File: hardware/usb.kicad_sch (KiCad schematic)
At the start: 0 parts

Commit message: added USB components, updated BOM, marked components that still needs references
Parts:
- added C266, C267, C268, C269, C270, C271: C, symbol Device:C
- added IC30: USB3340-EZK-TR, QFN50P500X500X100-33N-D, symbol payload-sym:USB3340-EZK-TR
- added IC31: TPS2051BDGN, SOP65P490X110-9N, symbol payload-sym:TPS2051BDGN
- added IC32: PTN5150AHXMP, PTN5150AHXMP, symbol payload-sym:PTN5150AHXMP
- added J1: USB-C_Mtconn_UBF31-0171, USB-C_Mtconn_UBF31-0171, symbol payload-sym:USB-C_Mtconn_UBF31-0171
- added R155, R156, R157, R158, R159, R160, R161, R162, R163, R164, R165: R_US, symbol Device:R_US
- added TP31, TP32, TP33, TP34: TestPoint, symbol Connector:TestPoint
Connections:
- new net: J1.A1 (GND), J1.A12 (GND), J1.B1 (GND), J1.B12 (GND)
- new net: J1.A4 (VBUS), J1.A9 (VBUS), J1.B4 (VBUS), J1.B9 (VBUS)
- new net: C267.1, IC32.4 (VBUS_DET), R163.1
- new net: IC30.1 (CLKOUT), R164.2
- new net: IC32.3 (PORT), R156.2, R162.1
- new net: C271.1, IC30.28 (VDD18), IC30.30 (NC_2)
- new net: C269.1, IC30.20 (VDD33)
- new net: IC30.24 (RBIAS), R165.2
- new net 3V3_USB0_RESETB: IC30.27 (RESETB)
- new net ADR/COM_DET: IC30.2 (NXT), IC32.5 (ADR/CON_DET), R157.2, R161.1, R164.1, TP31.1
- new net GNDREF: C266.2, C267.2, C268.2, C269.2, C270.2, C271.2, IC30.33 (EPAD), IC32.10 (GND), R161.2, R162.2, R165.1
- new net INTB/OUT3: IC30.3 (DATA0), IC32.6 (INTB/OUT3), R158.2, TP32.1
- new net SCL_OUT2: IC30.10 (DATA6), IC30.13 (DATA7), IC30.5 (DATA2), IC30.7 (DATA4), IC32.8 (SCL/OUT2), R160.2, TP34.1
- new net SDA_OUT1: IC30.4 (DATA1), IC30.6 (DATA3), IC30.9 (DATA5), IC32.7 (SDA/OUT1), R159.2, TP33.1
- new net SYS_5V: C270.1, IC30.21 (VBAT)
- new net USB0_CC1: IC32.1 (CC1)
- new net USB0_CC2: IC32.2 (CC2)
- new net USB0_DIR: IC30.31 (DIR)
- new net USB0_ID: IC30.23 (ID), IC32.9 (ID), R155.2
- new net USB0_STP: IC30.29 (STP)
- new net USB0_VBUS: IC30.22 (VBUS)
- new net USB_5V: R163.2
- new net VCC_3V3: C266.1, C268.1, IC30.32 (VDDIO), IC32.12 (VDD), R155.1, R156.1, R157.1, R158.1, R159.1, R160.1

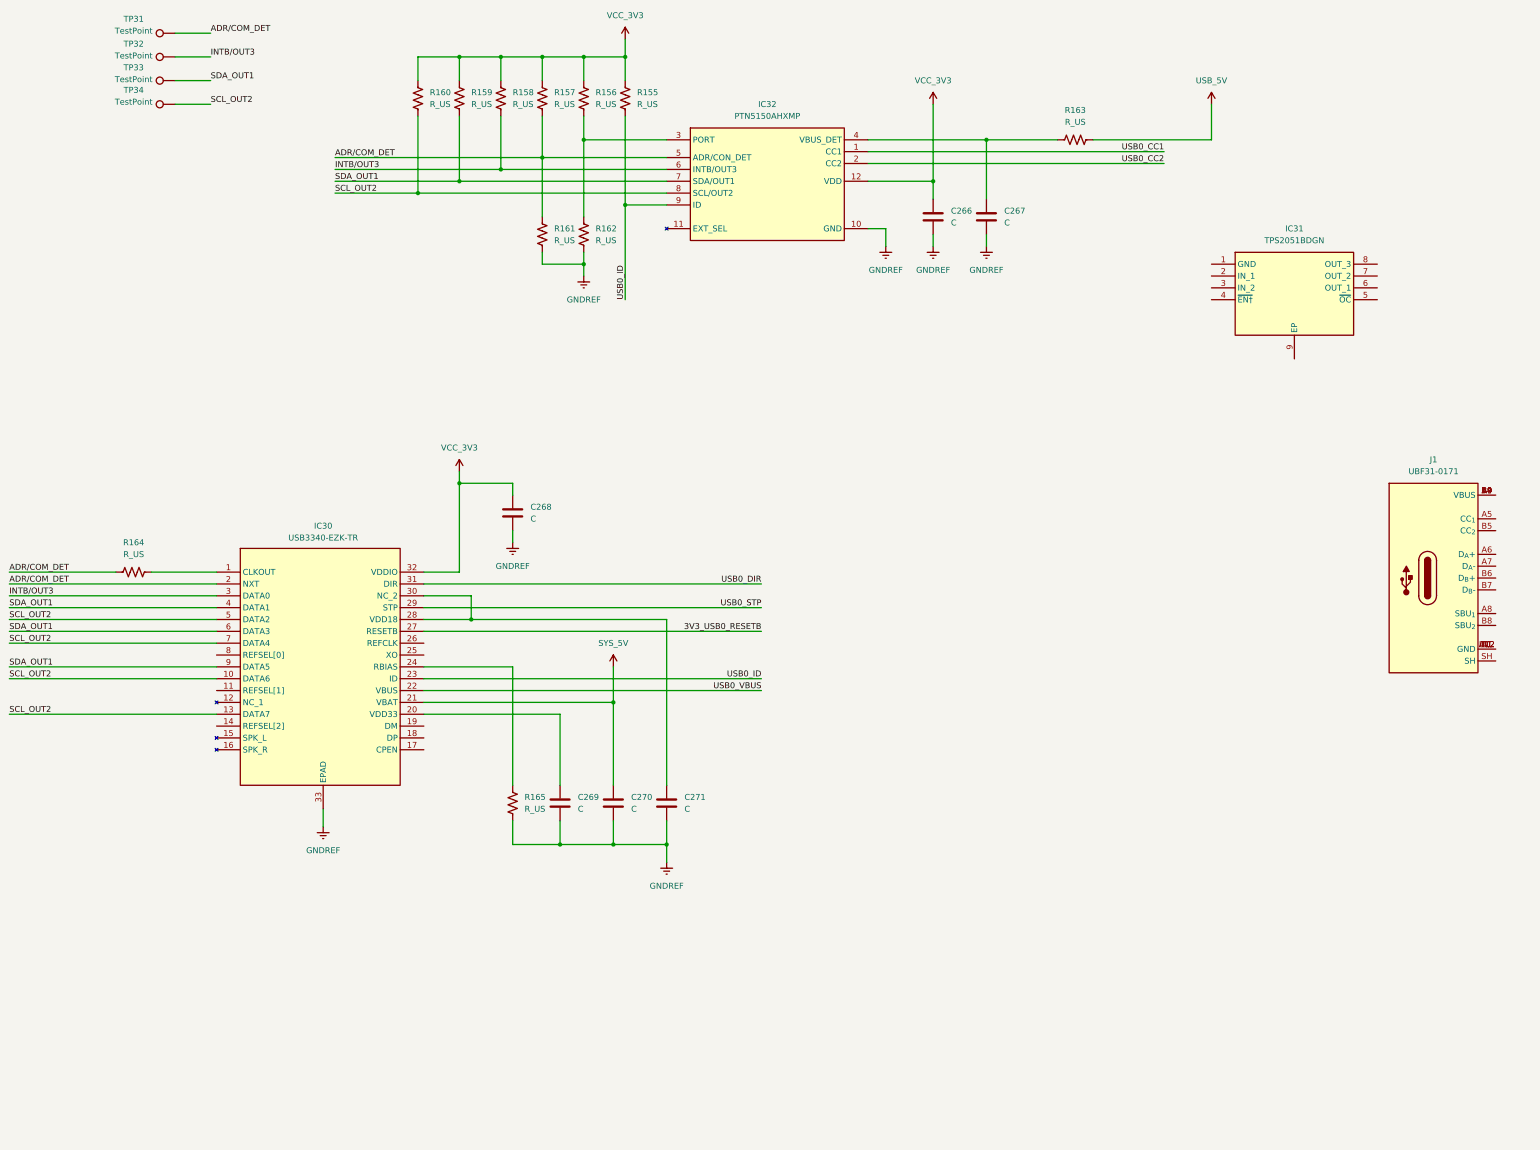
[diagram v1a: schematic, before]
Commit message: added usb devices in schematics
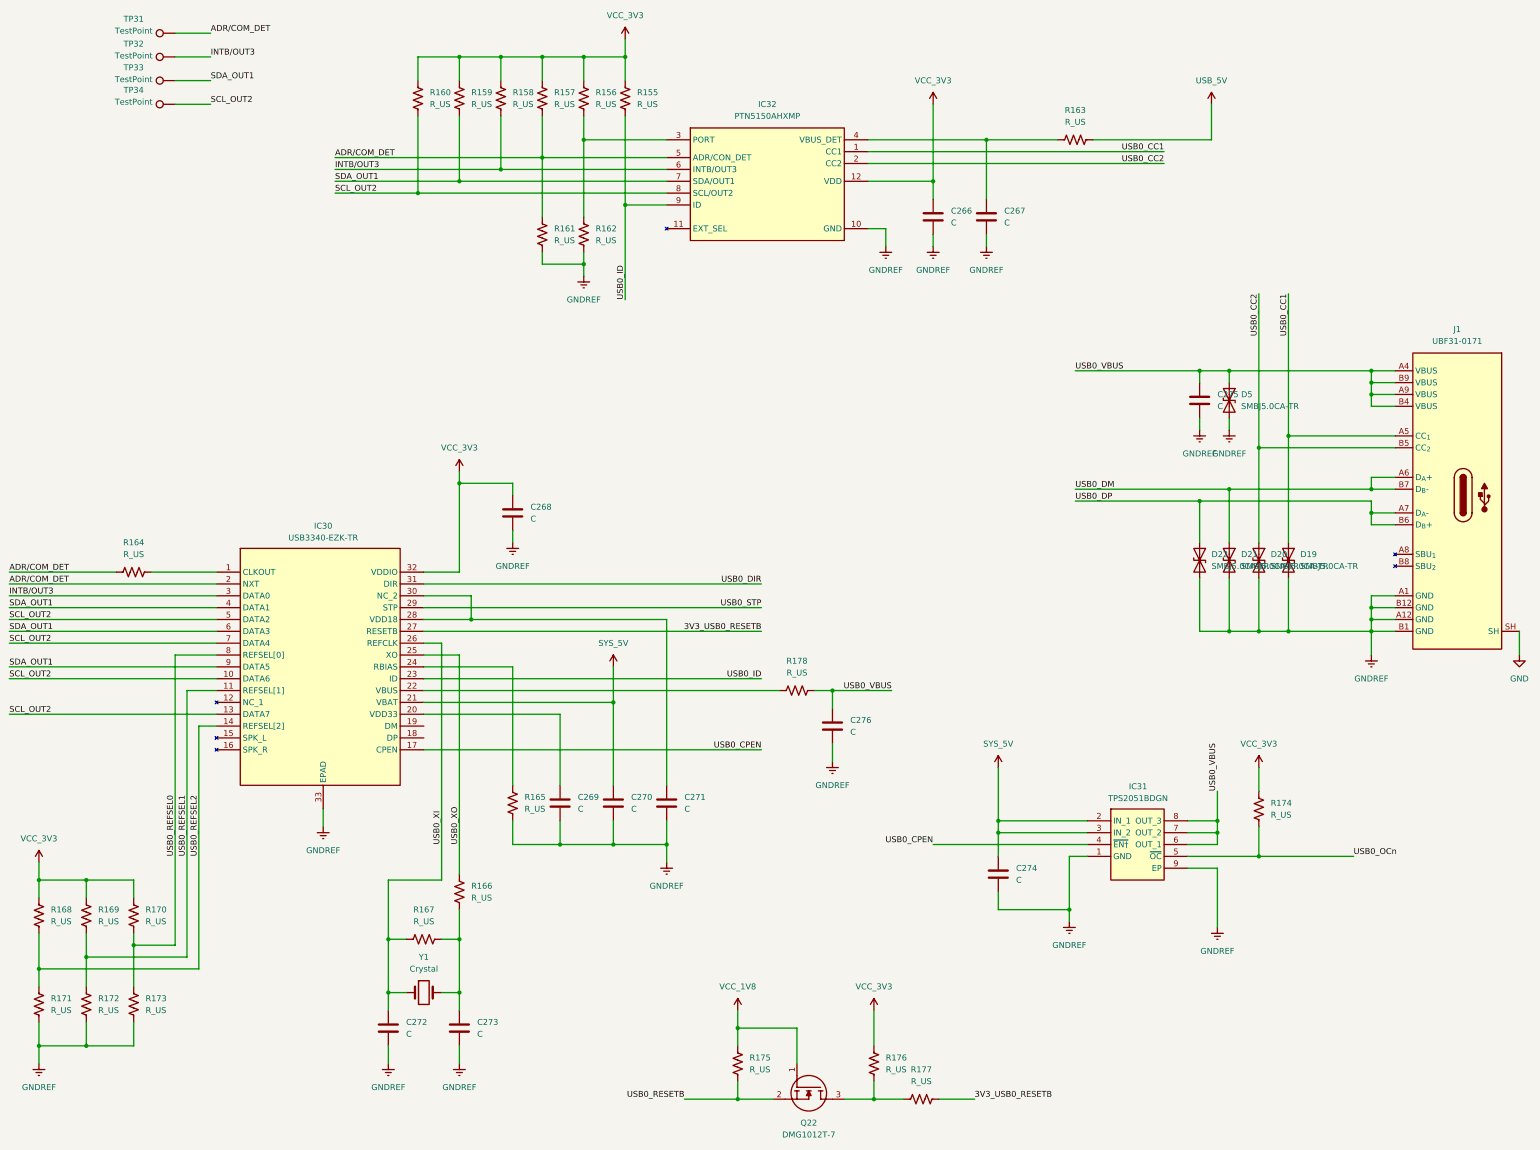
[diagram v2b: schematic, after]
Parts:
- added C272, C273, C274, C275, C276: C, symbol Device:C
- added D19, D20, D21, D22, D5: SMBJ5.0CA-TR, payload_footprints:SMBJ12A, symbol Device:D_TVS
- added Q22: DMG1012T-7, SOT50P160X90-3N, symbol payload-sym:DMG1012T-7
- added R166, R167, R168, R169, R170, R171, R172, R173, R174, R175, R176, R177, R178: R_US, symbol Device:R_US
- added Y1: Crystal, symbol Device:Crystal
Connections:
- net 3V3_USB0_RESETB: now also R177.1
- net GNDREF: now also IC31.1 (GND), IC31.9 (EP), J1.A1 (GND), J1.A12 (GND), J1.B1 (GND), J1.B12 (GND), C272.2, C273.2, C274.2, C275.2, C276.2, D19.2 (A2), D20.2 (A2), D21.2 (A2), D22.2 (A2), D5.2 (A2), R171.1, R172.1, R173.1
- net SYS_5V: now also IC31.2 (IN_1), IC31.3 (IN_2), C274.1
- net USB0_CC1: now also J1.A5 (CC_{1}), D19.1 (A1)
- net USB0_CC2: now also J1.B5 (CC_{2}), D20.1 (A1)
- net USB0_VBUS: now also IC31.6 (OUT_1), IC31.7 (OUT_2), IC31.8 (OUT_3), J1.A4 (VBUS), J1.A9 (VBUS), J1.B4 (VBUS), J1.B9 (VBUS), C275.1, C276.1, D5.1 (A1), R178.1; no longer IC30.22 (VBUS)
- net VCC_3V3: now also R168.2, R169.2, R170.2, R174.2, R176.2
- net USB0_DM: now reaches J1.A6 (D_{A}+)
- net USB0_DM: now also J1.B7 (D_{B}-), D21.1 (A1)
- net USB0_DP: now reaches J1.A7 (D_{A}-)
- net USB0_DP: now also J1.B6 (D_{B}+), D22.1 (A1)
- net GND: now reaches J1.SH
- net USB0_CPEN: now reaches IC31.4 (~{EN†})
- net USB0_CPEN: now also IC30.17 (CPEN)
- net USB0_OCn: now reaches IC31.5 (~{OC})
- net USB0_OCn: now also R174.1
- net USB0_REFSEL1: now reaches IC30.11 (REFSEL[1])
- net USB0_REFSEL1: now also R169.1, R172.2
- net USB0_REFSEL2: now reaches IC30.14 (REFSEL[2])
- net USB0_REFSEL2: now also R168.1, R171.2
- net USB0_XO: now reaches IC30.25 (XO)
- net USB0_XO: now also R166.2
- net USB0_XI: now reaches IC30.26 (REFCLK)
- net USB0_XI: now also C272.1, R167.2, Y1.1
- net USB0_REFSEL0: now reaches IC30.8 (REFSEL[0])
- net USB0_REFSEL0: now also R170.1, R173.2
- new net: Q22.3 (D), R176.1, R177.2
- new net: C273.1, R166.1, R167.1, Y1.2
- new net: IC30.22 (VBUS), R178.2
- new net USB0_RESETB: Q22.2 (S), R175.1
- new net VCC_1V8: Q22.1 (G), R175.2
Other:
- moved on the sheet: IC31

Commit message: assigned usb resistors and capacitors footprints, created a preliminary 3D PCB model
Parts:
- C266, C267, C268, C274: value C -> 100nF; footprint (none) -> payload_footprints:CAPC1005X55N
- C269, C270, C271: value C -> 1uF; footprint (none) -> payload_footprints:YAG_CC0402_YAG
- C272, C273: value C -> 18pF; footprint (none) -> payload_footprints:YAG_CC0402_YAG
- C275: value C -> 100uF; footprint (none) -> payload_footprints:CAPC3216X180N
- C276: value C -> 2.2uF; footprint (none) -> payload_footprints:CAP_CC0603_YAG
- R155, R156, R157, R158, R159, R160, R161, R162, R174, R175, R176: value R_US -> 10K; footprint (none) -> payload_footprints:RC0402N_YAG
- R163, R166, R169, R170, R171: value R_US -> 0R; footprint (none) -> payload_footprints:RC0402N_YAG
- R164: value R_US -> 27R; footprint (none) -> payload_footprints:RESC1005X40N
- R165: value R_US -> 8.06K; footprint (none) -> payload_footprints:RESC1005X40N
- R167: value R_US -> 1M; footprint (none) -> payload_footprints:RC0402N_YAG
- R168, R172, R173: value R_US -> DNP
- R177: value R_US -> 33R; footprint (none) -> payload_footprints:RC0402N_YAG
- R178: value R_US -> 1K; footprint (none) -> payload_footprints:RC0402N_YAG
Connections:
- net USB0_DM: now also IC30.19 (DM)
- net USB0_DP: now also IC30.18 (DP)
